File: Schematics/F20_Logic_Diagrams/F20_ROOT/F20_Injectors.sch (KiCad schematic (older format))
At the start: 4 parts

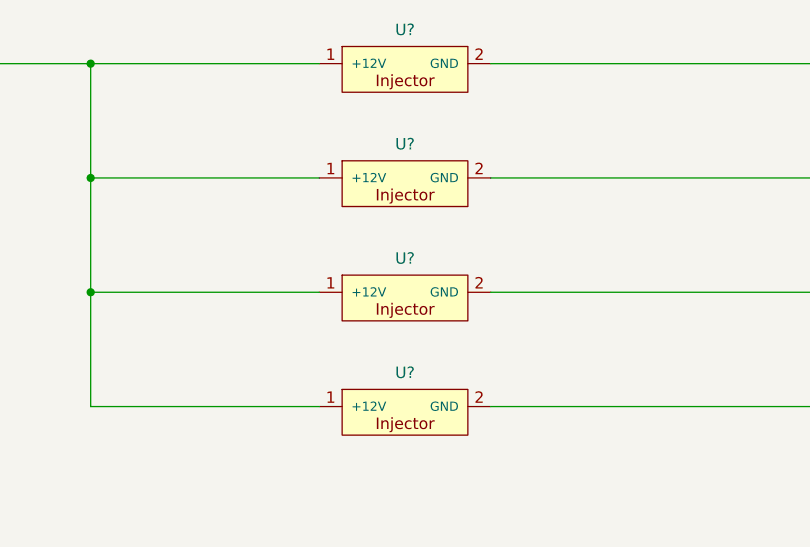
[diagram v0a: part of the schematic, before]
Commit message: Re-annotated Logic Diagrams, pulled a BOM list based on Logic Diagrams
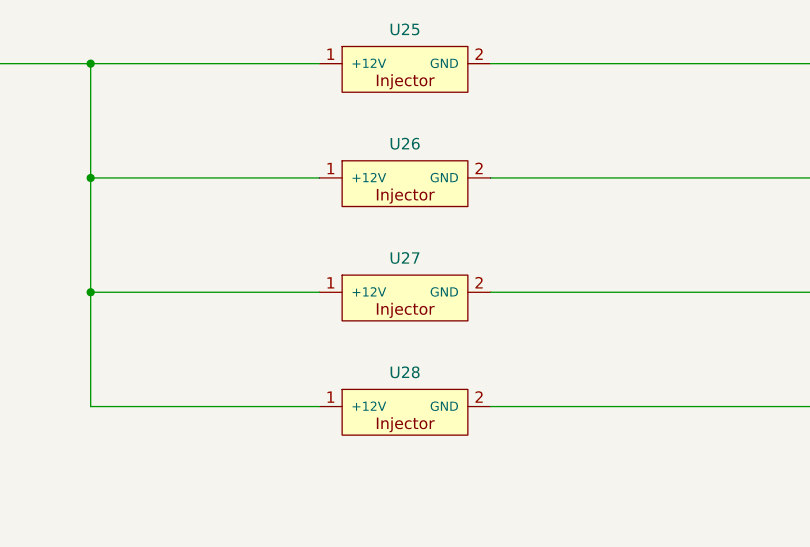
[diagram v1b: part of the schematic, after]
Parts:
- gave numbers to parts that had none: 4
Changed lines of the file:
@@
 INJECTORS_PWR
 $Comp
-L FSAE_Library:Injector U?
+L FSAE_Library:Injector U25
 U 1 1 5E568814
 P 5000 3000
-F 0 "U?" H 5375 3148 50  0000 C CNN
+F 0 "U25" H 5375 3148 50  0000 C CNN
 F 1 "Injector" H 5300 3150 50  0001 C CNN
 F 2 "" H 5300 3150 50  0001 C CNN
@@
 $EndComp
 $Comp
-L FSAE_Library:Injector U?
+L FSAE_Library:Injector U26
 U 1 1 5E5691B9
 P 5000 3500
-F 0 "U?" H 5375 3648 50  0000 C CNN
+F 0 "U26" H 5375 3648 50  0000 C CNN
 F 1 "Injector" H 5300 3650 50  0001 C CNN
 F 2 "" H 5300 3650 50  0001 C CNN
@@
 $EndComp
 $Comp
-L FSAE_Library:Injector U?
+L FSAE_Library:Injector U27
 U 1 1 5E569571
 P 5000 4000
-F 0 "U?" H 5375 4148 50  0000 C CNN
+F 0 "U27" H 5375 4148 50  0000 C CNN
 F 1 "Injector" H 5300 4150 50  0001 C CNN
 F 2 "" H 5300 4150 50  0001 C CNN
@@
 $EndComp
 $Comp
-L FSAE_Library:Injector U?
+L FSAE_Library:Injector U28
 U 1 1 5E569812
 P 5000 4500
-F 0 "U?" H 5375 4648 50  0000 C CNN
+F 0 "U28" H 5375 4648 50  0000 C CNN
 F 1 "Injector" H 5300 4650 50  0001 C CNN
 F 2 "" H 5300 4650 50  0001 C CNN
